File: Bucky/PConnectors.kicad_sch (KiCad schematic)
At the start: 25 parts, among them J1 XT60PW-M, J10 XT30AW-M, J11 XT30AW-M, J12 XT30AW-M, J13 XT30AW-M, J14 XT30AW-M, J2 XT90PW-M, J3 XT30PW-M, J4 XT30PW-M, J5 XT30PW-M, J6 XT30PW-M, J7 XT30AW-M, J8 XT30AW-M, J9 XT30AW-M

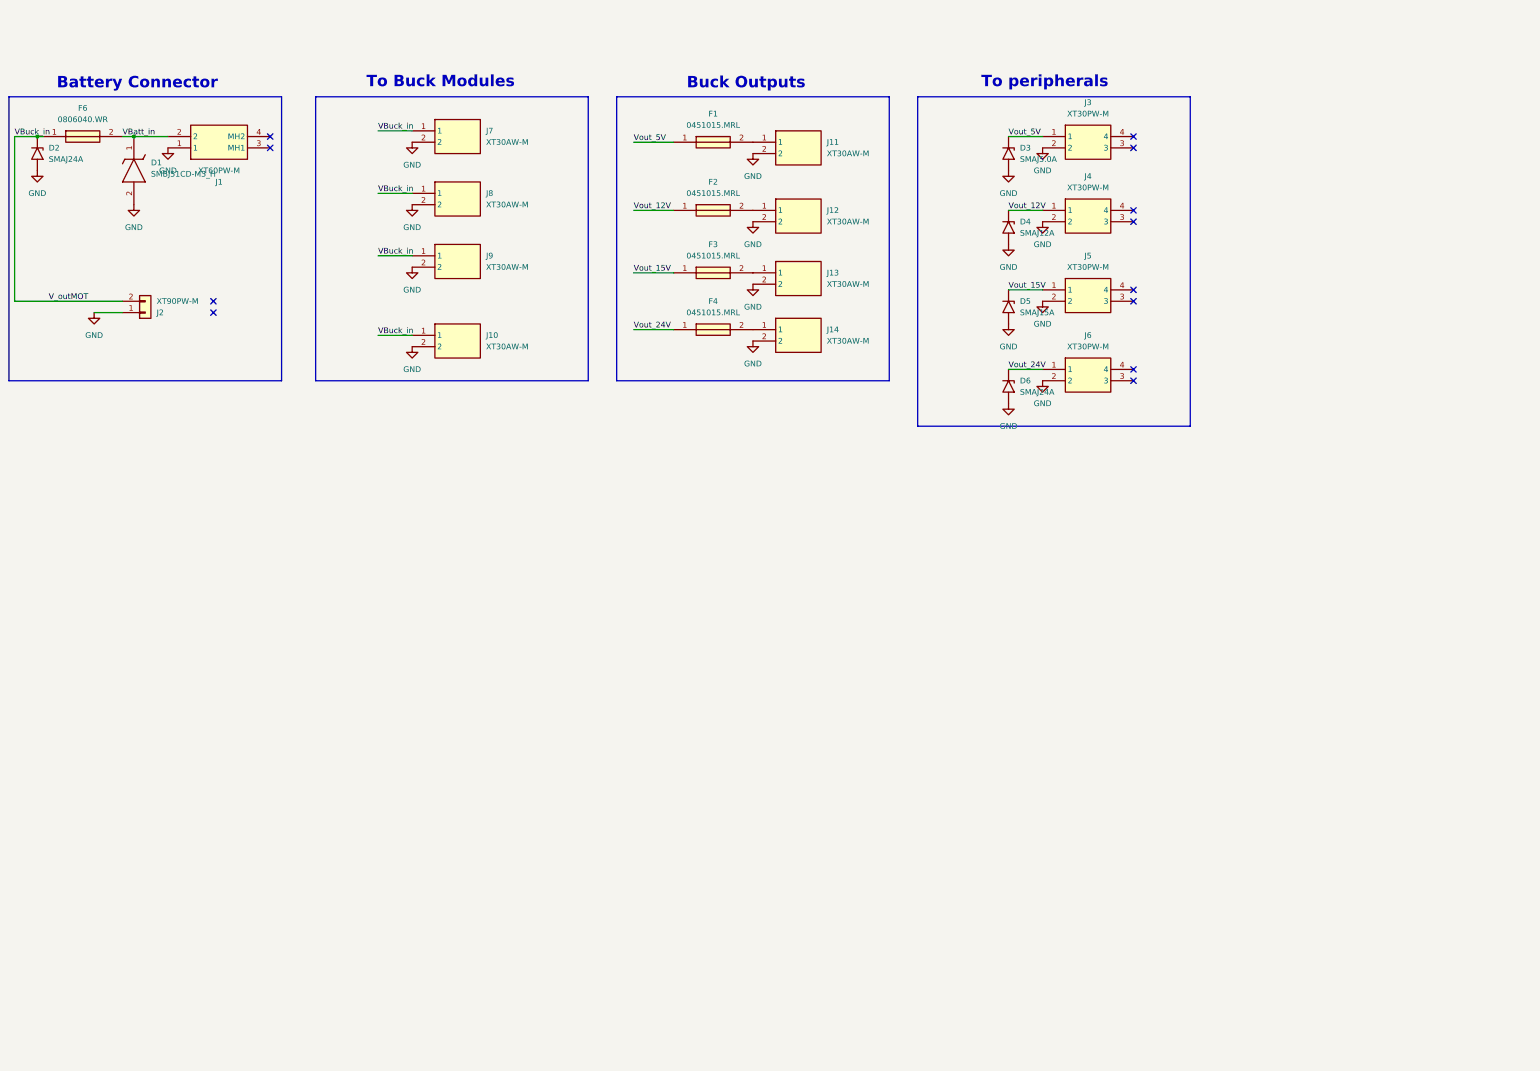
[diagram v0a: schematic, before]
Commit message: adapted schematics and added more protection from GEODE (Reverse Current)
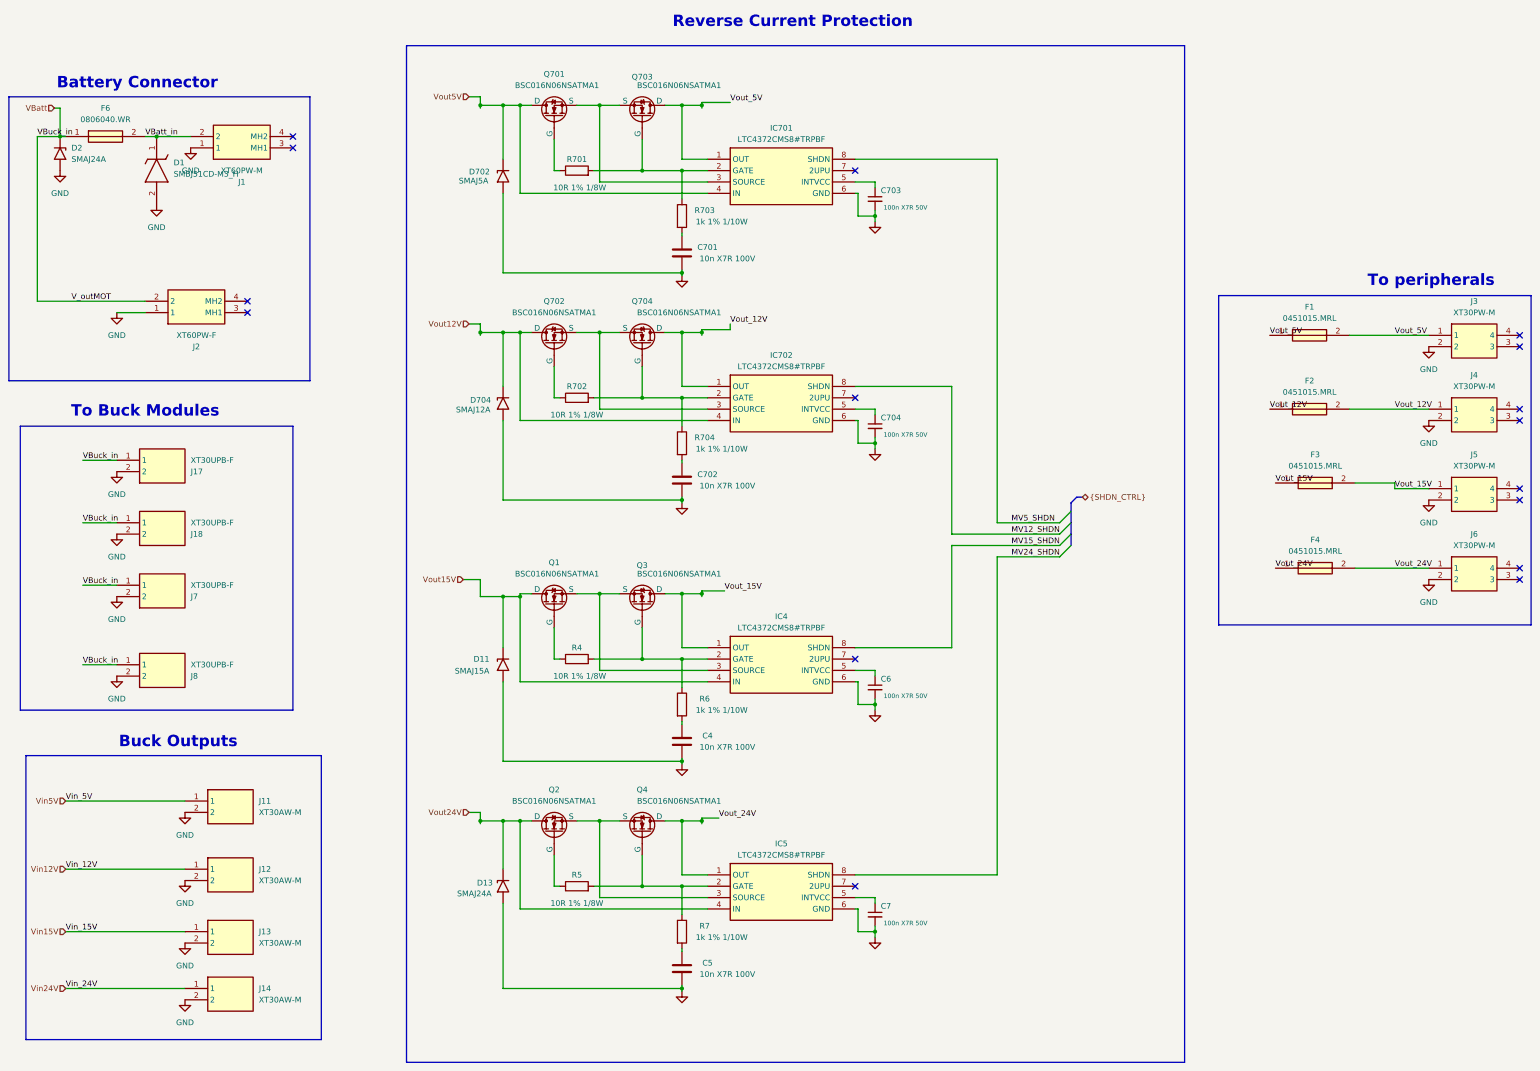
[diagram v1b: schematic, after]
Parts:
- removed D3: SMAJ5.0A, Diode_SMD:D_SMA, symbol Diode:SMAJ5.0A
- removed D4: SMAJ12A, Diode_SMD:D_SMA, symbol Diode:SMAJ12A
- removed D5: SMAJ15A, Diode_SMD:D_SMA, symbol Diode:SMAJ15A
- removed D6: SMAJ24A, Diode_SMD:D_SMA, symbol Diode:SMAJ24A
- removed J10, J7, J8, J9: XT30AW-M, SamacSys_Parts:XT30AWM, symbol SamacSys_Parts:XT30AW-M
- removed J2: XT90PW-M, 0_connectors:AMASS_XT90PW-M, symbol Connector_Generic:Conn_01x02
- added C4, C5, C701, C702: 10n X7R 100V, 0_capacitor_smd:C_0402_1005_DensityHigh, symbol Device:C
- added C6, C7, C703, C704: 100n X7R 50V, 0_capacitor_smd:C_0402_1005_DensityHigh, symbol Device:C_Small
- added D11: SMAJ15A, Diode_SMD:D_SMA, symbol Diode:SMAJ33A
- added D13: SMAJ24A, Diode_SMD:D_SMA, symbol Diode:SMAJ33A
- added D702: SMAJ5A, Diode_SMD:D_SMA, symbol Diode:SMAJ33A
- added D704: SMAJ12A, Diode_SMD:D_SMA, symbol Diode:SMAJ33A
- added IC4, IC5, IC701, IC702: LTC4372CMS8#TRPBF, 0_package_SOT_TO_SMD:SOP65P490X110-8N, symbol LTC4372CMS8#TRPBF:LTC4372CMS8#TRPBF
- added J17, J18, J7, J8: XT30UPB-F, XT30UPBF, symbol SamacSys_Parts:XT30UPB-F
- added J2: XT60PW-F, XT60PWF, symbol SamacSys_Parts:XT60PW-F
- added Q1, Q2, Q3, Q4, Q701, Q702, Q703, Q704: BSC016N06NSATMA1, 0_transistor_fet:PG-TDSON-8_INF, symbol Simulation_SPICE:NMOS
- added R4, R5, R701, R702: 10R 1% 1/8W, 0_resistor_smd:R_0805_2012_DensityHigh, symbol Device:R
- added R6, R7, R703, R704: 1k 1% 1/10W, 0_resistor_smd:R_0603_1608_DensityHigh, symbol Device:R
- F1, F2, F3, F4: footprint SamacSys_Parts:FUSC6127X294N -> FUSC6127X294N
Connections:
- net GND: now also C4.1, C5.1, C6.2, C7.2, C701.1, C702.1, C703.2, C704.2, D11.2 (A2), D13.2 (A2), D702.2 (A2), D704.2 (A2), IC4.6 (GND), IC5.6 (GND), IC701.6 (GND), IC702.6 (GND), J17.2, J18.2, J2.1, J7.2, J8.2
- net Vout_12V: now also F2.2, IC702.1 (OUT), Q704.1 (D)
- net Vout_15V: now also F3.2, IC4.1 (OUT), Q3.1 (D)
- net Vout_24V: now also F4.2, IC5.1 (OUT), Q4.1 (D)
- net Vout_5V: now also F1.2, IC701.1 (OUT), Q703.1 (D)
- net Vin15V: now reaches J13.1
- net Vin15V: no longer F3.2
- net Vin24V: now reaches J14.1
- net Vin24V: no longer F4.2
- net Vin12V: now reaches J12.1
- net Vin12V: no longer F2.2
- net Vin5V: now reaches J11.1
- net Vin5V: no longer F1.2
- net VBuck_in renamed VBatt
- net VBatt: now also J17.1, J18.1, J2.2, J7.1, J8.1
- new net: IC701.2 (GATE), Q703.2 (G), R701.2, R703.1
- new net: C701.2, R703.2
- new net: C4.2, R6.2
- new net: C702.2, R704.2
- new net: IC702.2 (GATE), Q704.2 (G), R702.2, R704.1
- new net: IC702.3 (SOURCE), Q702.3 (S), Q704.3 (S)
- new net: Q2.2 (G), R5.1
- new net: IC5.3 (SOURCE), Q2.3 (S), Q4.3 (S)
- new net: IC5.2 (GATE), Q4.2 (G), R5.2, R7.1
- new net: C5.2, R7.2
- new net: Q702.2 (G), R702.1
- new net: C703.1, IC701.5 (INTVCC)
- new net: IC701.3 (SOURCE), Q701.3 (S), Q703.3 (S)
- new net: IC4.2 (GATE), Q3.2 (G), R4.2, R6.1
- new net: IC4.3 (SOURCE), Q1.3 (S), Q3.3 (S)
- new net: Q1.2 (G), R4.1
- new net: Q701.2 (G), R701.1
- new net: C6.1, IC4.5 (INTVCC)
- new net: C7.1, IC5.5 (INTVCC)
- new net: C704.1, IC702.5 (INTVCC)
- new net MV12_SHDN: IC702.8 (SHDN)
- new net MV15_SHDN: IC4.8 (SHDN)
- new net MV24_SHDN: IC5.8 (SHDN)
- new net MV5_SHDN: IC701.8 (SHDN)
- new net Vout12V: D704.1 (A1), IC702.4 (IN), Q702.1 (D)
- new net Vout15V: D11.1 (A1), IC4.4 (IN), Q1.1 (D)
- new net Vout24V: D13.1 (A1), IC5.4 (IN), Q2.1 (D)
- new net Vout5V: D702.1 (A1), IC701.4 (IN), Q701.1 (D)
- no-connect marks 12 -> 16
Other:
- note added: "Reverse Current Protection"
- moved on the sheet: D1, D2, F6, J1, J11, J12, J13, J14, J3, J4, J5, J6

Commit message: upadated scchematics
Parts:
- removed D2: SMAJ24A, Diode_SMD:D_SMA, symbol Diode:SMAJ24A
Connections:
- net VBatt: no longer J17.1, J18.1, J2.2, J7.1, J8.1
- new net V_Batt: J17.1, J18.1, J2.2, J7.1, J8.1
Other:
- note added: "Control"
- moved on the sheet: D1, F6, J1, J11, J12, J13, J14, J17, J18, J2, J7, J8

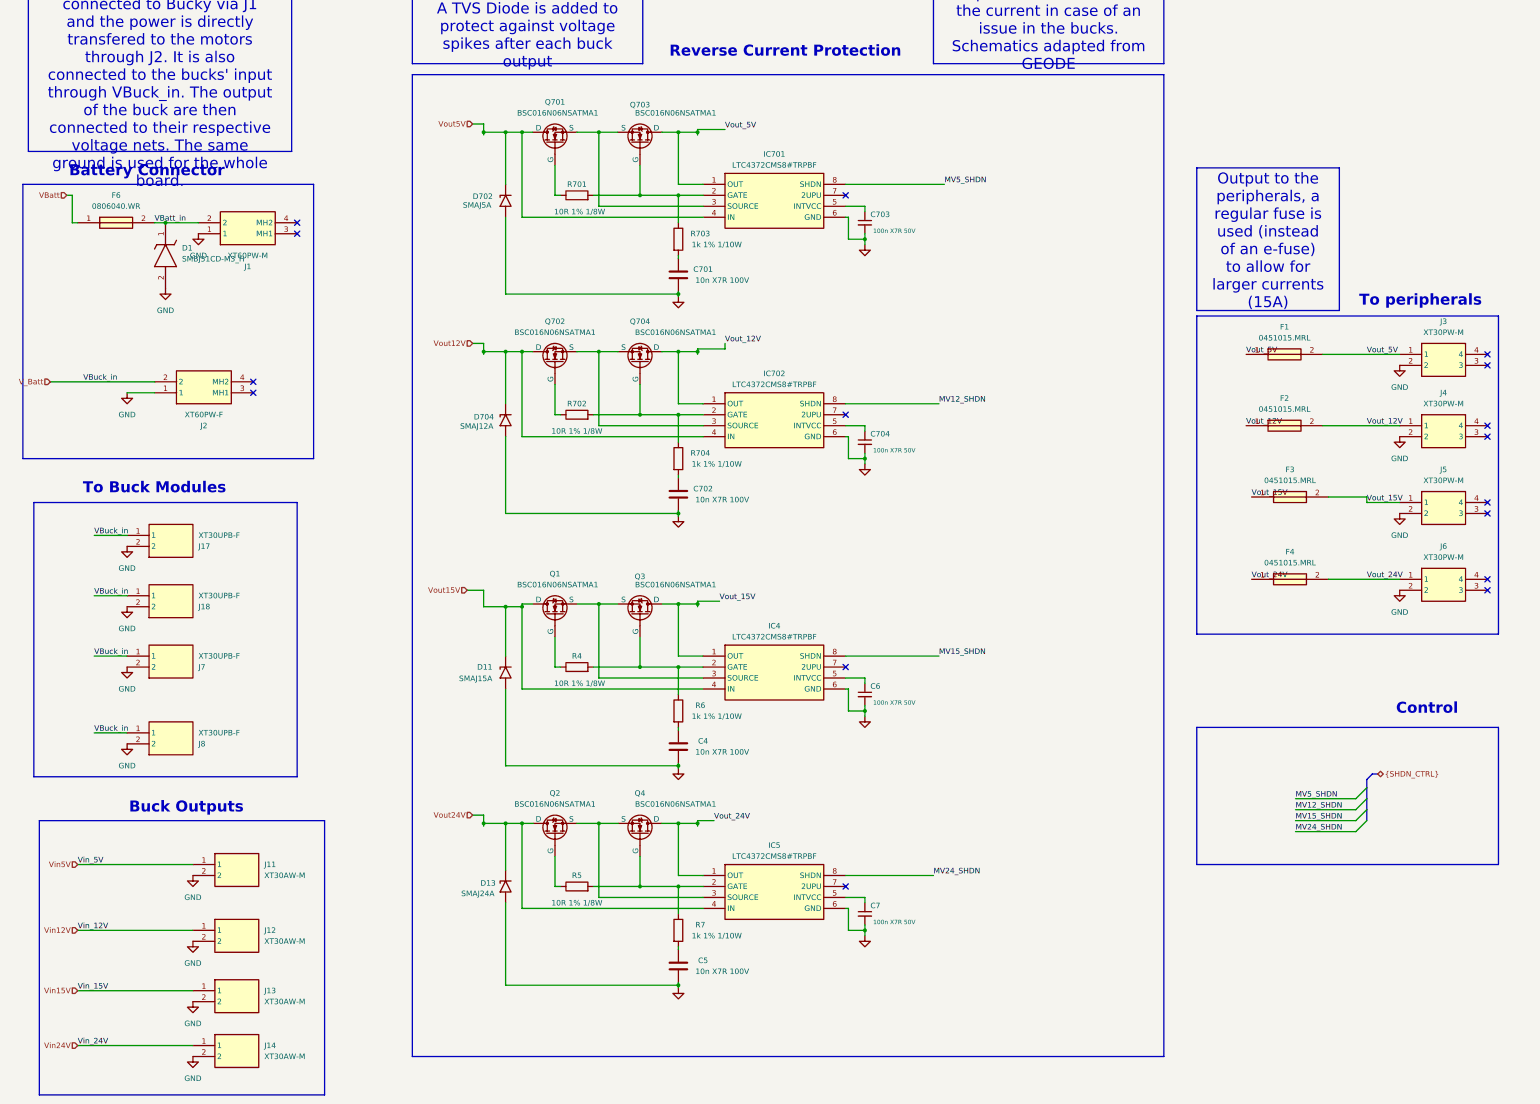
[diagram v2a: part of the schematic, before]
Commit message: changed high power transistors, started layout
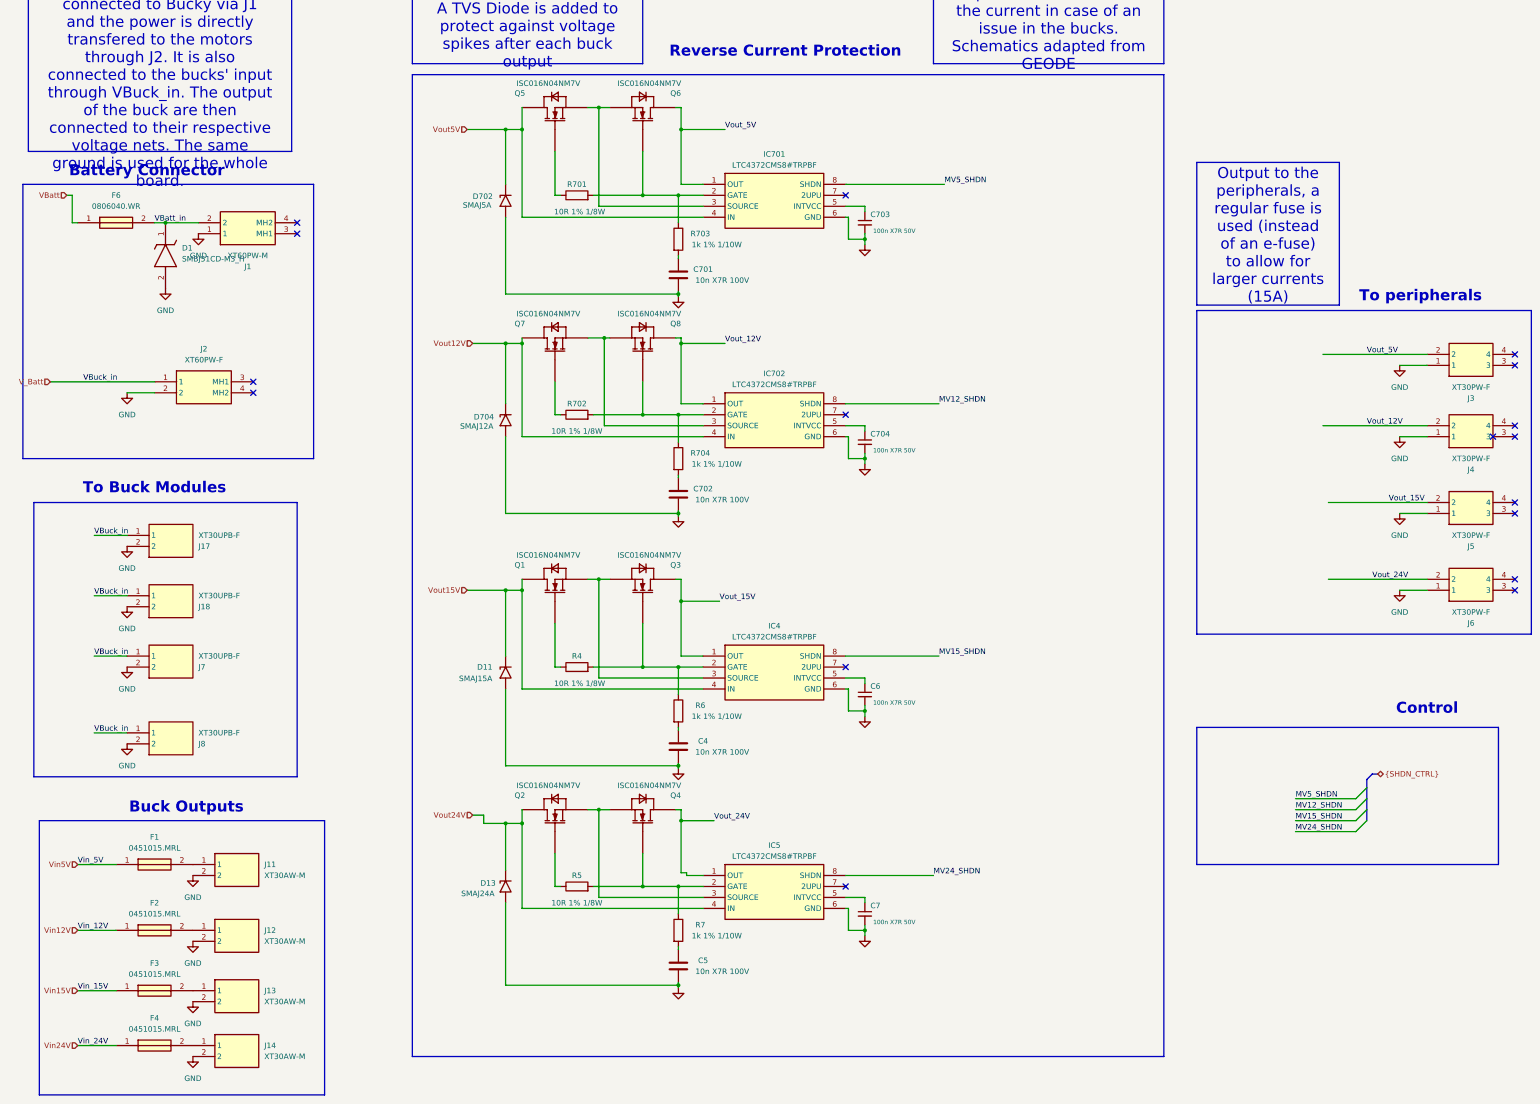
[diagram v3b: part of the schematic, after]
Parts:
- removed J3, J4, J5, J6: XT30PW-M, SamacSys_Parts:XT30PWM, symbol SamacSys_Parts:XT30PW-M
- removed Q1, Q2, Q3, Q4, Q701, Q702, Q703, Q704: BSC016N06NSATMA1, 0_transistor_fet:PG-TDSON-8_INF, symbol Simulation_SPICE:NMOS
- added J3, J4, J5, J6: XT30PW-F, XT30PWF, symbol SamacSys_Parts:XT30PW-F
- added Q1, Q2, Q3, Q4, Q5, Q6, Q7, Q8: ISC016N04NM7V, 0_transistor_fet:IFX-PG-TDSON-8-36-V, symbol ISC016N04NM7V:ISC016N04NM7V
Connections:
- net GND: now also J2.2, J3.1, J4.1, J5.1, J6.1; no longer J2.1
- net V_Batt: now also J2.1; no longer J2.2
- net Vin12V: now also F2.1; no longer J12.1
- net Vin15V: now also F3.1; no longer J13.1
- net Vin24V: now also F4.1; no longer J14.1
- net Vin5V: now also F1.1; no longer J11.1
- net Vout12V: now also Q7.5 (DRAIN_1), Q7.6 (DRAIN_2), Q7.7 (DRAIN_3), Q7.8 (DRAIN_4)
- net Vout15V: now also Q1.5 (DRAIN_1), Q1.6 (DRAIN_2), Q1.7 (DRAIN_3), Q1.8 (DRAIN_4)
- net Vout24V: now also Q2.5 (DRAIN_1), Q2.6 (DRAIN_2), Q2.7 (DRAIN_3), Q2.8 (DRAIN_4)
- net Vout5V: now also Q5.5 (DRAIN_1), Q5.6 (DRAIN_2), Q5.7 (DRAIN_3), Q5.8 (DRAIN_4)
- net Vout_12V: now also J4.2, Q8.5 (DRAIN_1), Q8.6 (DRAIN_2), Q8.7 (DRAIN_3), Q8.8 (DRAIN_4); no longer F2.1, F2.2
- net Vout_15V: now also J5.2, Q3.5 (DRAIN_1), Q3.6 (DRAIN_2), Q3.7 (DRAIN_3), Q3.8 (DRAIN_4); no longer F3.1, F3.2
- net Vout_24V: now also J6.2, Q4.5 (DRAIN_1), Q4.6 (DRAIN_2), Q4.7 (DRAIN_3), Q4.8 (DRAIN_4); no longer F4.1, F4.2
- net Vout_5V: now also J3.2, Q6.5 (DRAIN_1), Q6.6 (DRAIN_2), Q6.7 (DRAIN_3), Q6.8 (DRAIN_4); no longer F1.1, F1.2
- net at IC701.2 (GATE), R701.2, R703.1: now also Q6.4 (GATE)
- net at IC702.2 (GATE), R702.2, R704.1: now also Q8.4 (GATE)
- net at IC702.3 (SOURCE): now also Q7.1 (SOURCE_1), Q7.2 (SOURCE_2), Q7.3 (SOURCE_3), Q8.1 (SOURCE_1), Q8.2 (SOURCE_2), Q8.3 (SOURCE_3)
- net at R5.1: now also Q2.4 (GATE)
- net at IC5.3 (SOURCE): now also Q2.1 (SOURCE_1), Q2.2 (SOURCE_2), Q2.3 (SOURCE_3), Q4.1 (SOURCE_1), Q4.2 (SOURCE_2), Q4.3 (SOURCE_3)
- net at IC5.2 (GATE), R5.2, R7.1: now also Q4.4 (GATE)
- net at R702.1: now also Q7.4 (GATE)
- net at IC701.3 (SOURCE): now also Q5.1 (SOURCE_1), Q5.2 (SOURCE_2), Q5.3 (SOURCE_3), Q6.1 (SOURCE_1), Q6.2 (SOURCE_2), Q6.3 (SOURCE_3)
- net at IC4.2 (GATE), R4.2, R6.1: now also Q3.4 (GATE)
- net at IC4.3 (SOURCE): now also Q1.1 (SOURCE_1), Q1.2 (SOURCE_2), Q1.3 (SOURCE_3), Q3.1 (SOURCE_1), Q3.2 (SOURCE_2), Q3.3 (SOURCE_3)
- net at R4.1: now also Q1.4 (GATE)
- net at R701.1: now also Q5.4 (GATE)
- new net: F3.2, J13.1
- new net: F1.2, J11.1
- new net: F4.2, J14.1
- new net: F2.2, J12.1
- no-connect marks 16 -> 17
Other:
- moved on the sheet: F1, F2, F3, F4
